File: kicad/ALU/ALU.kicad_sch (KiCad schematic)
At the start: 3 parts, among them U1 74LS377, U2 74LS377, U3 74LS377

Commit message: Continue ALU work
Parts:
- added U10, U11, U12, U13, U14, U15, U16, U7, U8, U9: 74LS253, symbol 74xx:74LS253
- added U17, U18, U19, U20, U21: 74F382, symbol Custom:74F382
- added U22, U23, U24, U25, U26: 74LS283, symbol 74xx:74LS283
- added U27, U28, U29: 74LS244, symbol 74xx:74LS244
- added U4, U5, U6: 74LS377, symbol 74xx:74LS377
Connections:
- net +5V: now also U10.16 (VCC), U11.16 (VCC), U12.16 (VCC), U13.16 (VCC), U14.16 (VCC), U15.16 (VCC), U16.16 (VCC), U17.20 (VCC), U18.20 (VCC), U19.20 (VCC), U20.20 (VCC), U21.20 (VCC), U22.16 (VCC), U23.16 (VCC), U24.16 (VCC), U25.16 (VCC), U26.16 (VCC), U27.20 (VCC), U28.20 (VCC), U29.20 (VCC), U4.20 (VCC), U5.20 (VCC), U6.20 (VCC), U7.16 (VCC), U8.16 (VCC), U9.16 (VCC)
- net GND: now also U10.8 (GND), U11.8 (GND), U12.8 (GND), U13.8 (GND), U14.8 (GND), U15.8 (GND), U16.1 (OEa), U16.10 (I0b), U16.11 (I1b), U16.12 (I2b), U16.13 (I3b), U16.15 (OEb), U16.8 (GND), U17.10 (GND), U18.10 (GND), U19.10 (GND), U20.10 (GND), U21.10 (GND), U21.16 (B3), U21.17 (A3), U21.18 (B2), U22.11 (B4), U22.15 (B3), U22.2 (B2), U22.6 (B1), U22.8 (GND), U23.11 (B4), U23.15 (B3), U23.2 (B2), U23.6 (B1), U23.8 (GND), U24.11 (B4), U24.15 (B3), U24.2 (B2), U24.6 (B1), U24.8 (GND), U25.11 (B4), U25.15 (B3), U25.2 (B2), U25.6 (B1), U25.8 (GND), U26.11 (B4), U26.12 (A4), U26.14 (A3), U26.15 (B3), U26.2 (B2), U26.6 (B1), U26.8 (GND), U27.1 (OEa), U27.10 (GND), U27.19 (OEb), U28.1 (OEa), U28.10 (GND), U28.19 (OEb), U29.1 (OEa), U29.10 (GND), U29.11 (I0b), U29.13 (I1b), U29.15 (I2b), U29.17 (I3b), U29.19 (OEb), U29.6 (I2a), U29.8 (I3a), U4.10 (GND), U5.10 (GND), U6.10 (GND), U7.8 (GND), U8.8 (GND), U9.8 (GND)
- net CLK: now reaches U3.11 (CP)
- net CLK: now also U1.11 (CP), U2.11 (CP), U4.11 (CP), U5.11 (CP), U6.11 (CP)
- net OB16: now reaches U3.2 (Q0)
- net OB16: now also U14.10 (I0b), U14.4 (I2a), U15.11 (I1b), U16.3 (I3a), U21.3 (A0)
- net D16: now reaches U3.3 (D0)
- net D16: now also U15.7 (Za), U29.18 (O0a), U6.3 (D0)
- net D17: now reaches U3.4 (D1)
- net D17: now also U15.9 (Zb), U29.16 (O1a), U6.4 (D1)
- net OB17: now reaches U3.5 (Q1)
- net OB17: now also U14.12 (I2b), U15.6 (I0a), U16.5 (I1a), U21.1 (A1), U7.3 (I3a)
- net FLAG_LINK: now reaches U3.6 (Q2)
- net FLAG_LINK: now also U15.10 (I0b), U15.4 (I2a), U21.19 (A2), U7.13 (I3b), U7.5 (I1a)
- net OB4: now reaches U1.12 (Q4)
- net OB4: now also U10.3 (I3a), U18.3 (A0), U8.10 (I0b), U8.4 (I2a), U9.11 (I1b)
- net D4: now reaches U1.13 (D4)
- net D4: now also U27.9 (O0b), U4.13 (D4), U9.7 (Za)
- net D5: now reaches U1.14 (D5)
- net D5: now also U27.7 (O1b), U4.14 (D5), U9.9 (Zb)
- net OB5: now reaches U1.15 (Q5)
- net OB5: now also U10.13 (I3b), U10.5 (I1a), U18.1 (A1), U8.12 (I2b), U9.6 (I0a)
- net OB6: now reaches U1.16 (Q6)
- net OB6: now also U10.11 (I1b), U11.3 (I3a), U18.19 (A2), U9.10 (I0b), U9.4 (I2a)
- net D6: now reaches U1.17 (D6)
- net D6: now also U10.7 (Za), U27.5 (O2b), U4.17 (D6)
- net D7: now reaches U1.18 (D7)
- net D7: now also U10.9 (Zb), U27.3 (O3b), U4.18 (D7)
- net OB7: now reaches U1.19 (Q7)
- net OB7: now also U10.6 (I0a), U11.13 (I3b), U11.5 (I1a), U18.17 (A3), U9.12 (I2b)
- net OB0: now reaches U1.2 (Q0)
- net OB0: now also U15.12 (I2b), U16.6 (I0a), U17.3 (A0), U7.11 (I1b), U8.3 (I3a)
- net D0: now reaches U1.3 (D0)
- net D0: now also U27.18 (O0a), U4.3 (D0), U7.7 (Za)
- net D1: now reaches U1.4 (D1)
- net D1: now also U27.16 (O1a), U4.4 (D1), U7.9 (Zb)
- net OB1: now reaches U1.5 (Q1)
- net OB1: now also U16.4 (I2a), U17.1 (A1), U7.6 (I0a), U8.13 (I3b), U8.5 (I1a)
- net OB2: now reaches U1.6 (Q2)
- net OB2: now also U17.19 (A2), U7.10 (I0b), U7.4 (I2a), U8.11 (I1b), U9.3 (I3a)
- net D2: now reaches U1.7 (D2)
- net D2: now also U27.14 (O2a), U4.7 (D2), U8.7 (Za)
- net D3: now reaches U1.8 (D3)
- net D3: now also U27.12 (O3a), U4.8 (D3), U8.9 (Zb)
- net OB3: now reaches U1.9 (Q3)
- net OB3: now also U17.17 (A3), U7.12 (I2b), U8.6 (I0a), U9.13 (I3b), U9.5 (I1a)
- net OB12: now reaches U2.12 (Q4)
- net OB12: now also U12.10 (I0b), U12.4 (I2a), U13.11 (I1b), U14.3 (I3a), U20.3 (A0)
- net D12: now reaches U2.13 (D4)
- net D12: now also U13.7 (Za), U28.9 (O0b), U5.13 (D4)
- net D13: now reaches U2.14 (D5)
- net D13: now also U13.9 (Zb), U28.7 (O1b), U5.14 (D5)
- net OB13: now reaches U2.15 (Q5)
- net OB13: now also U12.12 (I2b), U13.6 (I0a), U14.13 (I3b), U14.5 (I1a), U20.1 (A1)
- net OB14: now reaches U2.16 (Q6)
- net OB14: now also U13.10 (I0b), U13.4 (I2a), U14.11 (I1b), U15.3 (I3a), U20.19 (A2)
- net D14: now reaches U2.17 (D6)
- net D14: now also U14.7 (Za), U28.5 (O2b), U5.17 (D6)
- net D15: now reaches U2.18 (D7)
- net D15: now also U14.9 (Zb), U28.3 (O3b), U5.18 (D7)
- net OB15: now reaches U2.19 (Q7)
- net OB15: now also U13.12 (I2b), U14.6 (I0a), U15.13 (I3b), U15.5 (I1a), U20.17 (A3)
- net OB8: now reaches U2.2 (Q0)
- net OB8: now also U10.10 (I0b), U10.4 (I2a), U11.11 (I1b), U12.3 (I3a), U19.3 (A0)
- net D8: now reaches U2.3 (D0)
- net D8: now also U11.7 (Za), U28.18 (O0a), U5.3 (D0)
- net D9: now reaches U2.4 (D1)
- net D9: now also U11.9 (Zb), U28.16 (O1a), U5.4 (D1)
- net OB9: now reaches U2.5 (Q1)
- net OB9: now also U10.12 (I2b), U11.6 (I0a), U12.13 (I3b), U12.5 (I1a), U19.1 (A1)
- net OB10: now reaches U2.6 (Q2)
- net OB10: now also U11.10 (I0b), U11.4 (I2a), U12.11 (I1b), U13.3 (I3a), U19.19 (A2)
- net D10: now reaches U2.7 (D2)
- net D10: now also U12.7 (Za), U28.14 (O2a), U5.7 (D2)
- net D11: now reaches U2.8 (D3)
- net D11: now also U12.9 (Zb), U28.12 (O3a), U5.8 (D3)
- net OB11: now reaches U2.9 (Q3)
- net OB11: now also U11.12 (I2b), U12.6 (I0a), U13.13 (I3b), U13.5 (I1a), U19.17 (A3)
- new net: U19.14 (Cout), U20.15 (Cn)
- new net: U18.14 (Cout), U19.15 (Cn)
- new net: U10.1 (OEa), U10.15 (OEb), U11.1 (OEa), U11.15 (OEb), U12.1 (OEa), U13.1 (OEa), U13.15 (OEb), U14.1 (OEa), U14.15 (OEb), U15.1 (OEa), U15.15 (OEb), U7.1 (OEa), U8.1 (OEa), U8.15 (OEb), U9.1 (OEa), U9.15 (OEb)
- new net: U20.14 (Cout), U21.15 (Cn)
- new net: U17.14 (Cout), U18.15 (Cn)
- new net: U22.9 (C4), U23.7 (C0)
- new net: U25.9 (C4), U26.7 (C0)
- new net: U23.9 (C4), U24.7 (C0)
- new net: U24.9 (C4), U25.7 (C0)
- new net AO0: U17.8 (F0), U22.5 (A1)
- new net AO1: U17.9 (F1), U22.3 (A2)
- new net AO10: U19.11 (F2), U24.14 (A3)
- new net AO11: U19.12 (F3), U24.12 (A4)
- new net AO12: U20.8 (F0), U25.5 (A1)
- new net AO13: U20.9 (F1), U25.3 (A2)
- new net AO14: U20.11 (F2), U25.14 (A3)
- new net AO15: U20.12 (F3), U25.12 (A4)
- new net AO16: U21.8 (F0), U26.5 (A1)
- new net AO17: U21.9 (F1), U26.3 (A2)
- new net AO2: U17.11 (F2), U22.14 (A3)
- new net AO3: U17.12 (F3), U22.12 (A4)
- new net AO4: U18.8 (F0), U23.5 (A1)
- new net AO5: U18.9 (F1), U23.3 (A2)
- new net AO6: U18.11 (F2), U23.14 (A3)
- new net AO7: U18.12 (F3), U23.12 (A4)
- new net AO8: U19.8 (F0), U24.5 (A1)
- new net AO9: U19.9 (F1), U24.3 (A2)
- new net AR0: U22.4 (S1), U27.2 (I0a)
- new net AR1: U22.1 (S2), U27.4 (I1a)
- new net AR10: U24.13 (S3), U28.6 (I2a)
- new net AR11: U24.10 (S4), U28.8 (I3a)
- new net AR12: U25.4 (S1), U28.11 (I0b)
- new net AR13: U25.1 (S2), U28.13 (I1b)
- new net AR14: U25.13 (S3), U28.15 (I2b)
- new net AR15: U25.10 (S4), U28.17 (I3b)
- new net AR16: U26.4 (S1), U29.2 (I0a)
- new net AR17: U26.1 (S2), U29.4 (I1a)
- new net AR2: U22.13 (S3), U27.6 (I2a)
- new net AR3: U22.10 (S4), U27.8 (I3a)
- new net AR4: U23.4 (S1), U27.11 (I0b)
- new net AR5: U23.1 (S2), U27.13 (I1b)
- new net AR6: U23.13 (S3), U27.15 (I2b)
- new net AR7: U23.10 (S4), U27.17 (I3b)
- new net AR8: U24.4 (S1), U28.2 (I0a)
- new net AR9: U24.1 (S2), U28.4 (I1a)
- new net MB0: U17.4 (B0)
- new net MB1: U17.2 (B1)
- new net MB10: U19.18 (B2)
- new net MB11: U19.16 (B3)
- new net MB12: U20.4 (B0)
- new net MB13: U20.2 (B1)
- new net MB14: U20.18 (B2)
- new net MB15: U20.16 (B3)
- new net MB16: U21.4 (B0)
- new net MB17: U21.2 (B1)
- new net MB2: U17.18 (B2)
- new net MB3: U17.16 (B3)
- new net MB4: U18.4 (B0)
- new net MB5: U18.2 (B1)
- new net MB6: U18.18 (B2)
- new net MB7: U18.16 (B3)
- new net MB8: U19.4 (B0)
- new net MB9: U19.2 (B1)
- no-connect marks 0 -> 27
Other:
- note added: "MB"
- note added: "OB"
- note added: "Register"
- moved on the sheet: U1, U2, U3

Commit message: Implement ALU arithmetic support logic
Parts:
- added U30: 74LS386, symbol 74xx:74LS386
- added U31: 74LS08, symbol 74xx:74LS08
- added U32: 74LS32, symbol 74xx:74LS32
- added U33: 74LS04, symbol 74xx:74LS04
- added U34: 74LS253, symbol 74xx:74LS253
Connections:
- net +5V: now also U34.16 (VCC)
- net AR17: now also U30.5
- net FLAG_LINK: now also U30.1, U32.9, U33.11, U34.6 (I0a)
- net GND: now also U3.13 (D4), U3.14 (D5), U3.17 (D6), U3.18 (D7), U3.8 (D3), U6.14 (D5), U6.17 (D6), U6.18 (D7), U34.1 (OEa), U34.10 (I0b), U34.11 (I1b), U34.12 (I2b), U34.13 (I3b), U34.15 (OEb), U34.8 (GND)
- net MB17: now also U30.9
- net OB17: now also U30.6, U33.3
- net at U3.7 (D2): now also U34.7 (Za)
- net ALUO0: now reaches U19.5 (S0)
- net ALUO0: now also U10.14 (A0), U11.14 (A0), U12.14 (A0), U13.14 (A0), U14.14 (A0), U15.14 (A0), U16.14 (A0), U17.5 (S0), U18.5 (S0), U20.5 (S0), U21.5 (S0), U7.14 (A0), U8.14 (A0), U9.14 (A0), U31.5
- net ALUO1: now reaches U19.6 (S1)
- net ALUO1: now also U10.2 (A1), U11.2 (A1), U12.2 (A1), U13.2 (A1), U14.2 (A1), U15.2 (A1), U16.2 (A1), U17.6 (S1), U18.6 (S1), U20.6 (S1), U21.6 (S1), U7.2 (A1), U8.2 (A1), U9.2 (A1), U31.4
- net ALUO2: now reaches U19.7 (S2)
- net ALUO2: now also U17.7 (S2), U18.7 (S2), U20.7 (S2), U21.7 (S2), U32.1
- net at U10.1 (OEa), U10.15 (OEb), U11.1 (OEa)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: now also U12.15 (OEb)
- net ARITH_CARRY_OUT: now reaches U21.11 (F2)
- net ARITH_CARRY_OUT: now also U30.2, U33.9
- net at U17.15 (Cn): now also U33.2
- net at U22.7 (C0): now also U31.3
- net at U16.7 (Za): now also U34.3 (I3a)
- new net: U30.10, U31.10
- new net: U30.8, U33.4
- new net: U31.8, U32.10
- new net: U31.13, U32.8
- new net: U30.4, U31.9
- new net: U33.10, U34.5 (I1a)
- new net: U32.6, U34.4 (I2a)
- new net: U30.3, U32.2
- new net: U32.11, U33.5
- new net: U32.4, U33.6
- new net: U32.12, U33.8
- new net: U31.2, U32.3
- new net: U31.6, U33.1
- new net: U31.11, U32.5
- new net LINK_SEL_0: U34.14 (A0)
- new net LINK_SEL_1: U34.2 (A1)
- new net ONES_COMP_SELECT: U31.1, U31.12, U32.13
- no-connect marks 27 -> 26
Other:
- note added: "Arithmetic link output select"
- note added: "Carry in if subtracting"
- note added: "Ones-complement overflow"
- note added: "Post-increment enable"

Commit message: Implement OB zero flag logic
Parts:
- added R1: 1K, symbol Device:R
- added U35, U36: 74LS27, symbol 74xx:74LS27
- added U37: 74LS11, symbol 74xx:74LS11
- added U38: 74LS257, symbol 74xx:74LS257
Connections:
- net +5V: now also R1.1, U38.16 (VCC)
- net GND: now also U38.8 (GND)
- net OB0: now also U35.1
- net OB1: now also U35.2
- net OB10: now also U36.2
- net OB11: now also U36.13
- net OB12: now also U36.3
- net OB13: now also U36.4
- net OB14: now also U36.5
- net OB15: now also U36.9
- net OB16: now also U36.10
- net OB17: now also U36.11
- net OB2: now also U35.13
- net OB3: now also U35.3
- net OB4: now also U35.4
- net OB5: now also U35.5
- net OB6: now also U35.9
- net OB7: now also U35.10
- net OB8: now also U35.11
- net OB9: now also U36.1
- net LINK_SEL_0 renamed LINKS0
- net LINK_SEL_1 renamed LINKS1
- new net: U36.8, U37.5
- new net: R1.2, U37.9
- new net: U35.12, U37.1
- new net: U36.12, U37.3
- new net: U36.6, U37.4
- new net: U37.11, U37.6
- new net: U35.6, U37.2
- new net: U37.10, U37.12
- new net: U35.8, U37.13
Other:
- moved on the sheet: U30D

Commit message: Start work on control board
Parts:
- added C1, C10, C11, C12, C13, C14, C15, C16, C17, C18, C19, C2, C20, C21, C22, C23, C24, C25, C26, C27, C28, C29, C3, C30, C31, C32, C33, C34, C35, C36, C37, C38, C39, C4, C5, C6, C7, C8, C9: 0.1uF, symbol Device:C
- added C20: 100 uF, Capacitor_THT:CP_Radial_D6.3mm_P2.50mm, symbol Device:C_Polarized
- added J1: Backplane Signal, symbol Connector_Generic:Conn_02x30_Odd_Even
- added J2: Backplane Bus, symbol Connector_Generic:Conn_02x20_Odd_Even
- added R2: 4.7K, symbol Device:R
- added U39: 74LS32, symbol 74xx:74LS32
- R1: value 1K -> 4.7K
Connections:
- net +5V: now also U30.14 (VCC), U31.14 (VCC), U32.14 (VCC), U33.14 (VCC), U35.14 (VCC), U36.14 (VCC), U37.14 (VCC), C1.1, C10.1, C11.1, C12.1, C13.1, C14.1, C15.1, C16.1, C17.1, C18.1, C19.1, C2.1, C20.1, C20.1, C21.1, C22.1, C23.1, C24.1, C25.1, C26.1, C27.1, C28.1, C29.1, C3.1, C30.1, C31.1, C32.1, C33.1, C34.1, C35.1, C36.1, C37.1, C38.1, C39.1, C4.1, C5.1, C6.1, C7.1, C8.1, C9.1, J1.2 (Pin_2), J1.59 (Pin_59), J2.2 (Pin_2), J2.39 (Pin_39), R2.1, U39.14 (VCC)
- net ALUO0: now also J1.42 (Pin_42)
- net ALUO1: now also J1.44 (Pin_44)
- net ALUO2: now also J1.46 (Pin_46)
- net AR4: now also U38.11 (I0d); no longer U27.11 (I0b)
- net CLK: now also J1.56 (Pin_56)
- net D0: now also J2.3 (Pin_3)
- net D1: now also J2.5 (Pin_5)
- net D10: now also J2.23 (Pin_23)
- net D11: now also J2.25 (Pin_25)
- net D12: now also J2.27 (Pin_27)
- net D13: now also J2.29 (Pin_29)
- net D14: now also J2.31 (Pin_31)
- net D15: now also J2.33 (Pin_33)
- net D16: now also J2.35 (Pin_35)
- net D17: now also J2.37 (Pin_37)
- net D2: now also J2.7 (Pin_7)
- net D3: now also J2.9 (Pin_9)
- net D4: now also J2.11 (Pin_11)
- net D5: now also J2.13 (Pin_13)
- net D6: now also J2.15 (Pin_15)
- net D7: now also J2.17 (Pin_17)
- net D8: now also J2.19 (Pin_19)
- net D9: now also J2.21 (Pin_21)
- net FLAG_LINK: now also J1.10 (Pin_10)
- net GND: now also U30.12, U30.13, U30.7 (GND), U31.7 (GND), U32.7 (GND), U33.7 (GND), U35.7 (GND), U36.7 (GND), U37.7 (GND), U38.15 (OE), U38.2 (I0a), U38.3 (I1a), C1.2, C10.2, C11.2, C12.2, C13.2, C14.2, C15.2, C16.2, C17.2, C18.2, C19.2, C2.2, C20.2, C20.2, C21.2, C22.2, C23.2, C24.2, C25.2, C26.2, C27.2, C28.2, C29.2, C3.2, C30.2, C31.2, C32.2, C33.2, C34.2, C35.2, C36.2, C37.2, C38.2, C39.2, C4.2, C5.2, C6.2, C7.2, C8.2, C9.2, J1.1 (Pin_1), J1.60 (Pin_60), J2.1 (Pin_1), J2.40 (Pin_40), U39.10, U39.12, U39.13, U39.7 (GND), U39.9; no longer U27.1 (OEa), U27.19 (OEb), U28.1 (OEa), U28.19 (OEb), U29.1 (OEa), U29.19 (OEb)
- net LINKS0: now also J1.48 (Pin_48)
- net LINKS1: now also J1.50 (Pin_50)
- net MB0: now also U4.2 (Q0)
- net MB1: now also U4.5 (Q1)
- net MB10: now also U5.6 (Q2)
- net MB11: now also U5.9 (Q3)
- net MB12: now also U5.12 (Q4)
- net MB13: now also U5.15 (Q5)
- net MB14: now also U5.16 (Q6)
- net MB15: now also U5.19 (Q7)
- net MB16: now also U6.2 (Q0)
- net MB17: now also U6.5 (Q1)
- net MB2: now also U4.6 (Q2)
- net MB3: now also U4.9 (Q3)
- net MB4: now also U4.12 (Q4)
- net MB5: now also U4.15 (Q5)
- net MB6: now also U4.16 (Q6)
- net MB7: now also U4.19 (Q7)
- net MB8: now also U5.2 (Q0)
- net MB9: now also U5.5 (Q1)
- net OB17: now also J1.8 (Pin_8)
- net *LATCH_MB: now reaches U5.1 (~{E})
- net *LATCH_MB: now also U4.1 (~{E}), U6.1 (~{E}), J1.37 (Pin_37)
- net *LATCH_OB: now reaches U3.1 (~{E})
- net *LATCH_OB: now also U1.1 (~{E}), U2.1 (~{E}), J1.41 (Pin_41)
- net at U3.7 (D2), U34.7 (Za): now also U38.6 (I1b)
- net at U10.1 (OEa), U10.15 (OEb), U11.1 (OEa)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: now also U7.15 (OEb), U39.6
- net FLAG_ZERO: now reaches U37.8
- net FLAG_ZERO: now also J1.6 (Pin_6)
- net at U33.12: now also U39.5
- net ALU_SHIFT: now reaches U33.13
- net ALU_SHIFT: now also J1.52 (Pin_52), U39.1
- net CTL_CONST: now reaches U38.1 (S)
- net CTL_CONST: now also J1.53 (Pin_53)
- net at U38.10 (I1d): now also R2.2
- net FLAG_AC_SIGN: now reaches U38.12 (Zc)
- net FLAG_AC_SIGN: now also U6.8 (D3), J1.14 (Pin_14)
- net at U38.13 (I1c): now also U38.5 (I0b), U6.6 (Q2)
- net at U38.14 (I0c): now also U6.9 (Q3)
- net FLAG_LINK_INIT: now reaches U38.7 (Zb)
- net FLAG_LINK_INIT: now also U6.7 (D2), J1.12 (Pin_12)
- net at U38.9 (Zd): now also U27.11 (I0b)
- net *IOT_SKIP_L: now reaches U6.12 (Q4)
- net *IOT_SKIP_L: now also J1.23 (Pin_23)
- net *IOT_SKIP: now reaches U6.13 (D4)
- net *IOT_SKIP: now also J1.19 (Pin_19)
- net ONES_COMP_SELECT renamed ALU_ONES
- net ALU_ONES: now also J1.54 (Pin_54)
- new net: U27.1 (OEa), U27.19 (OEb), U28.1 (OEa), U28.19 (OEb), U29.1 (OEa), U29.19 (OEb), U39.3
- new net *CHAN_REQ: J1.13 (Pin_13)
- new net *DEV_REQ: J1.15 (Pin_15)
- new net *DMA_REQ: J1.11 (Pin_11)
- new net *INT_REQ: J1.17 (Pin_17)
- new net *IOT_WAIT: J1.21 (Pin_21)
- new net *LATCH_AC: J1.31 (Pin_31)
- new net *LATCH_IR: J1.25 (Pin_25)
- new net *LATCH_MA: J1.27 (Pin_27)
- new net *LATCH_MQ: J1.35 (Pin_35)
- new net *LATCH_PC: J1.29 (Pin_29)
- new net *LATCH_STEP: J1.33 (Pin_33)
- new net *LATCH_WRTBK: J1.39 (Pin_39)
- new net *MEMM_ENABLE: J1.7 (Pin_7)
- new net *PI_ENABLE: J1.5 (Pin_5)
- new net *PROT_ENABLE: J1.9 (Pin_9)
- new net *RESET: J1.55 (Pin_55)
- new net *SELECT_ALU: J1.22 (Pin_22), U39.2, U39.4
- new net *SELECT_CORE: J1.24 (Pin_24)
- new net *SELECT_EXTRN: J1.28 (Pin_28)
- new net *SELECT_SWR: J1.26 (Pin_26)
- new net A0: J2.4 (Pin_4)
- new net A1: J2.6 (Pin_6)
- new net A10: J2.24 (Pin_24)
- new net A11: J2.26 (Pin_26)
- new net A12: J2.28 (Pin_28)
- new net A13: J2.30 (Pin_30)
- new net A14: J2.32 (Pin_32)
- new net A2: J2.8 (Pin_8)
- new net A3: J2.10 (Pin_10)
- new net A4: J2.12 (Pin_12)
- new net A5: J2.14 (Pin_14)
- new net A6: J2.16 (Pin_16)
- new net A7: J2.18 (Pin_18)
- new net A8: J2.20 (Pin_20)
- new net A9: J2.22 (Pin_22)
- new net ADDR_MODE0: J1.49 (Pin_49)
- new net ADDR_MODE1: J1.51 (Pin_51)
- new net BUS_SELECT0: J1.16 (Pin_16)
- new net BUS_SELECT1: J1.18 (Pin_18)
- new net BUS_SELECT2: J1.20 (Pin_20)
- new net DRQ_GRANT: J1.32 (Pin_32)
- new net HALT: J1.47 (Pin_47)
- new net INT_DETECT: J1.38 (Pin_38)
- new net IOT_PULSE: J1.30 (Pin_30)
- new net JMP_I_DETECT: J1.36 (Pin_36)
- new net READ_IN_PULSE: J1.40 (Pin_40)
- new net REQ_ADDR: J1.34 (Pin_34)
- new net SELECT_PCMA: J1.45 (Pin_45)
- new net STEP_ZERO: J1.4 (Pin_4)
- new net WRITE_CORE: J1.43 (Pin_43)
- no-connect marks 26 -> 85
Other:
- note added: "OB zero detect"
- moved on the sheet: R1, U1, U10, U11, U12, U13, U14, U15, U16, U17, U18, U19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

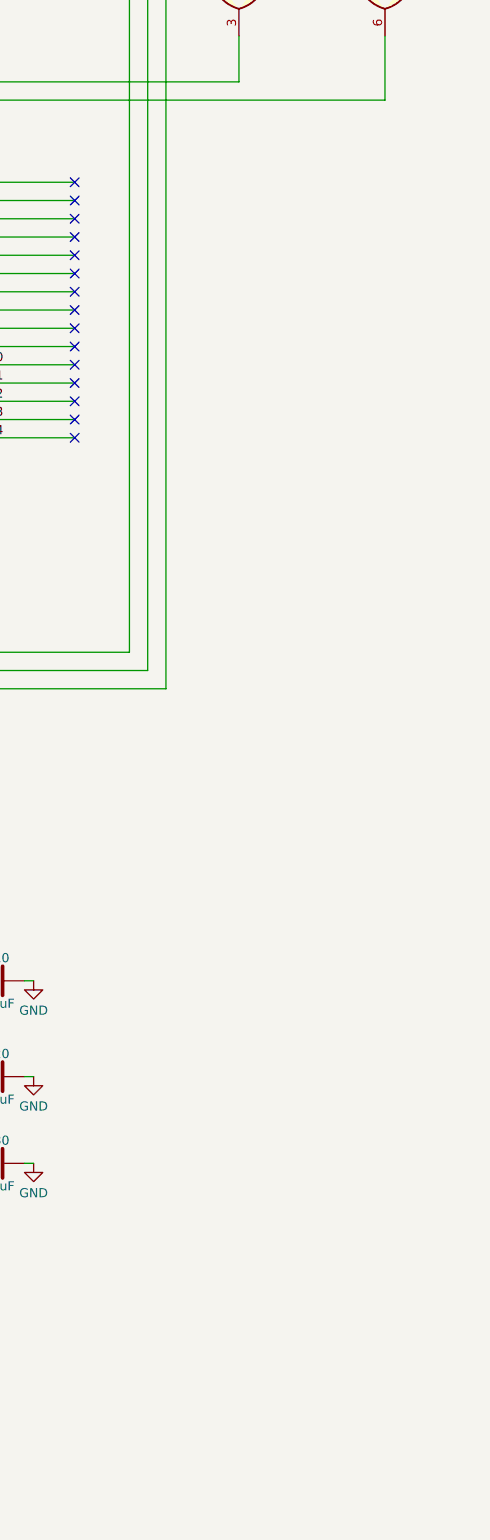
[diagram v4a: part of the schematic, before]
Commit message: Start migrating over to DIN41612 connectors
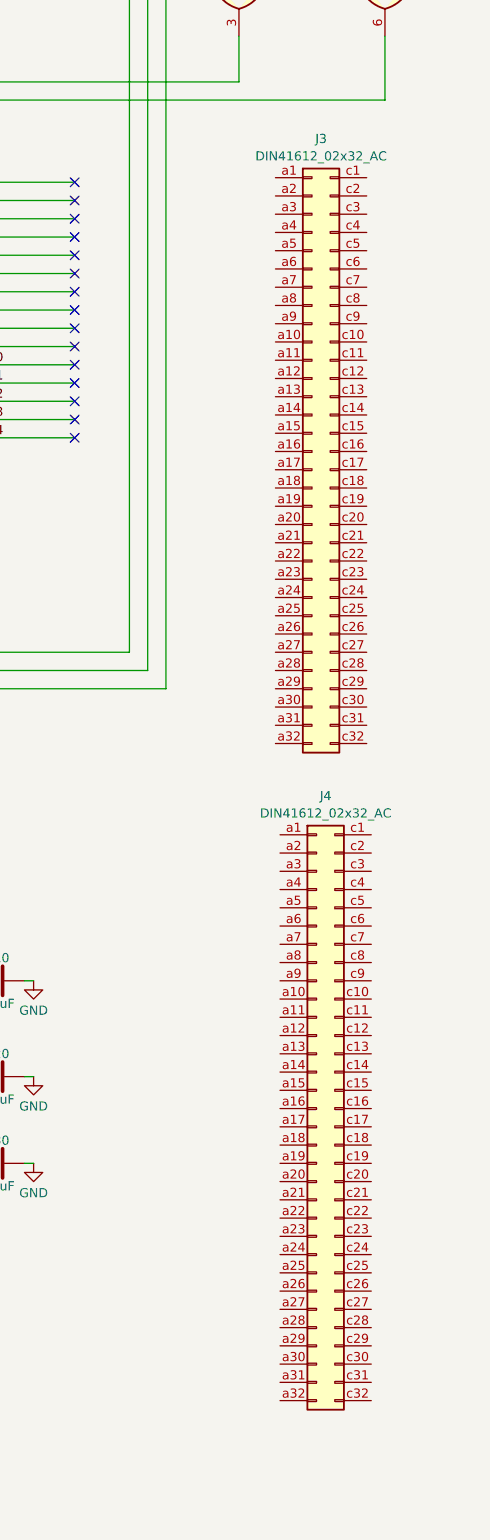
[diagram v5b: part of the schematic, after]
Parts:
- added J3, J4: DIN41612_02x32_AC, symbol Connector:DIN41612_02x32_AC
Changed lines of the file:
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@@
     )
   )
+  (symbol (lib_id "Connector:DIN41612_02x32_AC") (at 560.705 252.095 0) (unit 1)
+    (in_bom yes) (on_board yes) (dnp no) (fields_autoplaced)
+    (property "Reference" "J4" (at 561.975 208.5807 0)
+      (effects (font (size 1.27 1.27)))
+    )
+    (property "Value" "DIN41612_02x32_AC" (at 561.975 211.0049 0)
+      (effects (font (size 1.27 1.27)))
+    )
+    (property "Footprint" "" (at 560.705 252.095 0)
+      (effects (font (size 1.27 1.27)) hide)
+    )
+    (property "Datasheet" "~" (at 560.705 252.095 0)
+      (effects (font (size 1.27 1.27)) hide)
+    )
+    (pin "a1")
+    (pin "a10")
+    (pin "a11")
+    (pin "a12")
+    (pin "a13")
+    (pin "a14")
+    (pin "a15")
+    (pin "a16")
+    (pin "a17")
+    (pin "a18")
+    (pin "a19")
+    (pin "a2")
+    (pin "a20")
+    (pin "a21")
+    (pin "a22")
+    (pin "a23")
+    (pin "a24")
+    (pin "a25")
+    (pin "a26")
+    (pin "a27")
+    (pin "a28")
+    (pin "a29")
+    (pin "a3")
+    (pin "a30")
+    (pin "a31")
+    (pin "a32")
+    (pin "a4")
+    (pin "a5")
+    (pin "a6")
+    (pin "a7")
+    (pin "a8")
+    (pin "a9")
+    (pin "c1")
+    (pin "c10")
+    (pin "c11")
+    (pin "c12")
+    (pin "c13")
+    (pin "c14")
+    (pin "c15")
+    (pin "c16")
+    (pin "c17")
+    (pin "c18")
+    (pin "c19")
+    (pin "c2")
+    (pin "c20")
+    (pin "c21")
+    (pin "c22")
+    (pin "c23")
+    (pin "c24")
+    (pin "c25")
+    (pin "c26")
+    (pin "c27")
+    (pin "c28")
+    (pin "c29")
+    (pin "c3")
+    (pin "c30")
+    (pin "c31")
+    (pin "c32")
+    (pin "c4")
+    (pin "c5")
+    (pin "c6")
+    (pin "c7")
+    (pin "c8")
+    (pin "c9")
+    (instances
+      (project "ALU"
+        (path "/b26dce39-0c19-4808-8ddd-74847f21ad13"
+          (reference "J4") (unit 1)
+        )
+      )
+    )
+  )
   (symbol (lib_id "power:+5V") (at 363.22 115.57 0) (unit 1)
     (in_bom yes) (on_board yes) (dnp no) (fields_autoplaced)
@@
         )
       )
+    )
+  )
+  (symbol (lib_id "Connector:DIN41612_02x32_AC") (at 560.07 160.655 0) (unit 1)
+    (in_bom yes) (on_board yes) (dnp no) (fields_autoplaced)
+    (property "Reference" "J3" (at 561.34 117.1407 0)
+      (effects (font (size 1.27 1.27)))
+    )
+    (property "Value" "DIN41612_02x32_AC" (at 561.34 119.5649 0)
+      (effects (font (size 1.27 1.27)))
+    )
+    (property "Footprint" "" (at 560.07 160.655 0)
+      (effects (font (size 1.27 1.27)) hide)
+    )
+    (property "Datasheet" "~" (at 560.07 160.655 0)
+      (effects (font (size 1.27 1.27)) hide)
+    )
+    (pin "a1")
+    (pin "a10")
+    (pin "a11")
+    (pin "a12")
+    (pin "a13")
+    (pin "a14")
+    (pin "a15")
+    (pin "a16")
+    (pin "a17")
+    (pin "a18")
+    (pin "a19")
+    (pin "a2")
+    (pin "a20")
+    (pin "a21")
+    (pin "a22")
+    (pin "a23")
+    (pin "a24")
+    (pin "a25")
+    (pin "a26")
+    (pin "a27")
+    (pin "a28")
+    (pin "a29")
+    (pin "a3")
+    (pin "a30")
+    (pin "a31")
+    (pin "a32")
+    (pin "a4")
+    (pin "a5")
+    (pin "a6")
+    (pin "a7")
+    (pin "a8")
+    (pin "a9")
+    (pin "c1")
+    (pin "c10")
+    (pin "c11")
+    (pin "c12")
+    (pin "c13")
+    (pin "c14")
+    (pin "c15")
+    (pin "c16")
+    (pin "c17")
+    (pin "c18")
+    (pin "c19")
+    (pin "c2")
+    (pin "c20")
+    (pin "c21")
+    (pin "c22")
+    (pin "c23")
+    (pin "c24")
+    (pin "c25")
+    (pin "c26")
+    (pin "c27")
+    (pin "c28")
+    (pin "c29")
+    (pin "c3")
+    (pin "c30")
+    (pin "c31")
+    (pin "c32")
+    (pin "c4")
+    (pin "c5")
+    (pin "c6")
+    (pin "c7")
+    (pin "c8")
+    (pin "c9")
+    (instances
+      (project "ALU"
+        (path "/b26dce39-0c19-4808-8ddd-74847f21ad13"
+          (reference "J3") (unit 1)
+        )
+      )
